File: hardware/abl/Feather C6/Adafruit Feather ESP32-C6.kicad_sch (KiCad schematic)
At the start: 43 parts, among them Q3 DMG3415U, SW1 KMR2, SW2 KMR2, U1 ESP32-C6-MINI_MINI, U2 AP2112/RT9080-3.3, U3 MCP73831T-2ACI/OT, U4 AHT20-F, U5 AP2112/RT9080-3.3, X1 JSTPH, X2 MAX17048/T, X3 USB C

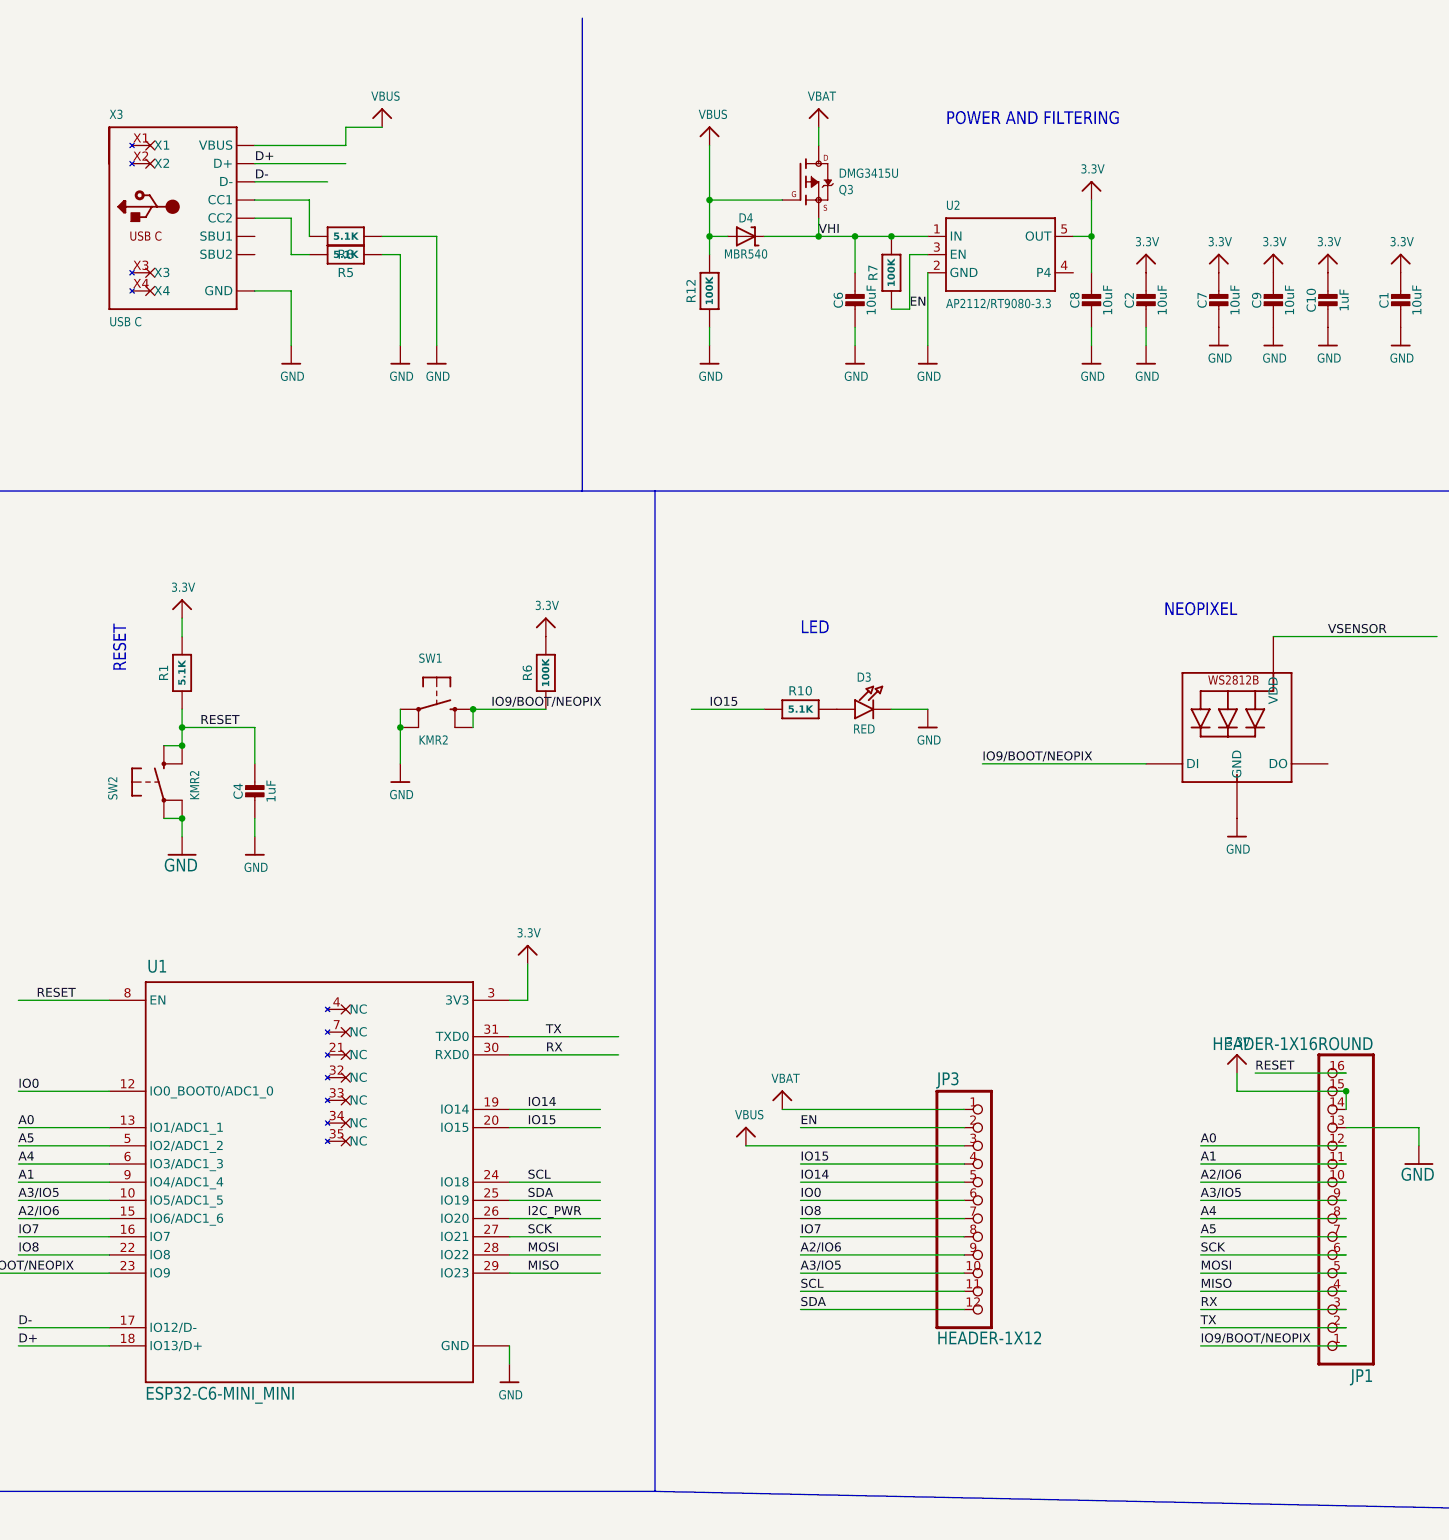
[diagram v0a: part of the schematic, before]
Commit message: Add ground planes and more ground pins.
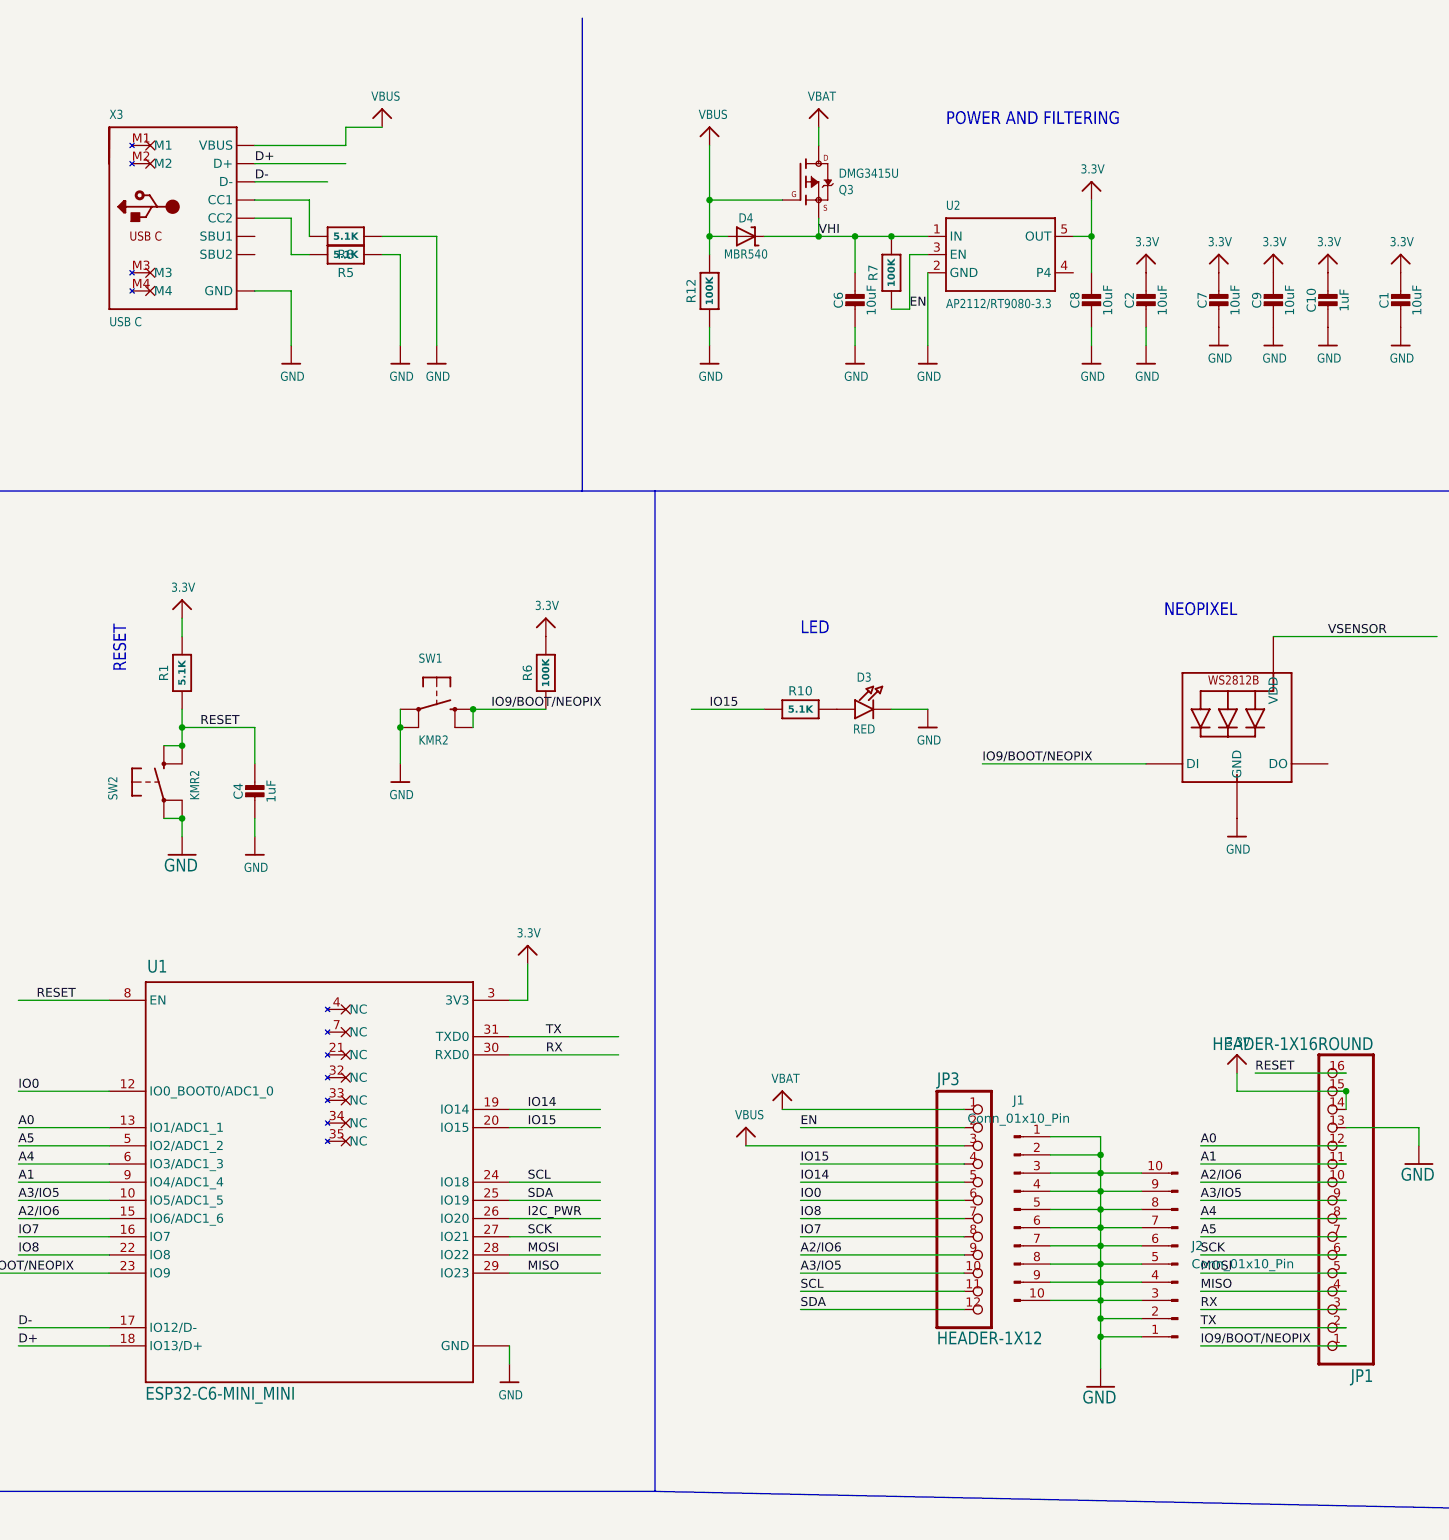
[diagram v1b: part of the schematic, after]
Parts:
- added J1, J2: Conn_01x10_Pin, Connector_PinHeader_2.54mm:PinHeader_1x10_P2.54mm_Vertical, symbol Connector:Conn_01x10_Pin
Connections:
- net GND: now also J1.1 (Pin_1), J1.10 (Pin_10), J1.2 (Pin_2), J1.3 (Pin_3), J1.4 (Pin_4), J1.5 (Pin_5), J1.6 (Pin_6), J1.7 (Pin_7), J1.8 (Pin_8), J1.9 (Pin_9), J2.1 (Pin_1), J2.10 (Pin_10), J2.2 (Pin_2), J2.3 (Pin_3), J2.4 (Pin_4), J2.5 (Pin_5), J2.6 (Pin_6), J2.7 (Pin_7), J2.8 (Pin_8), J2.9 (Pin_9)

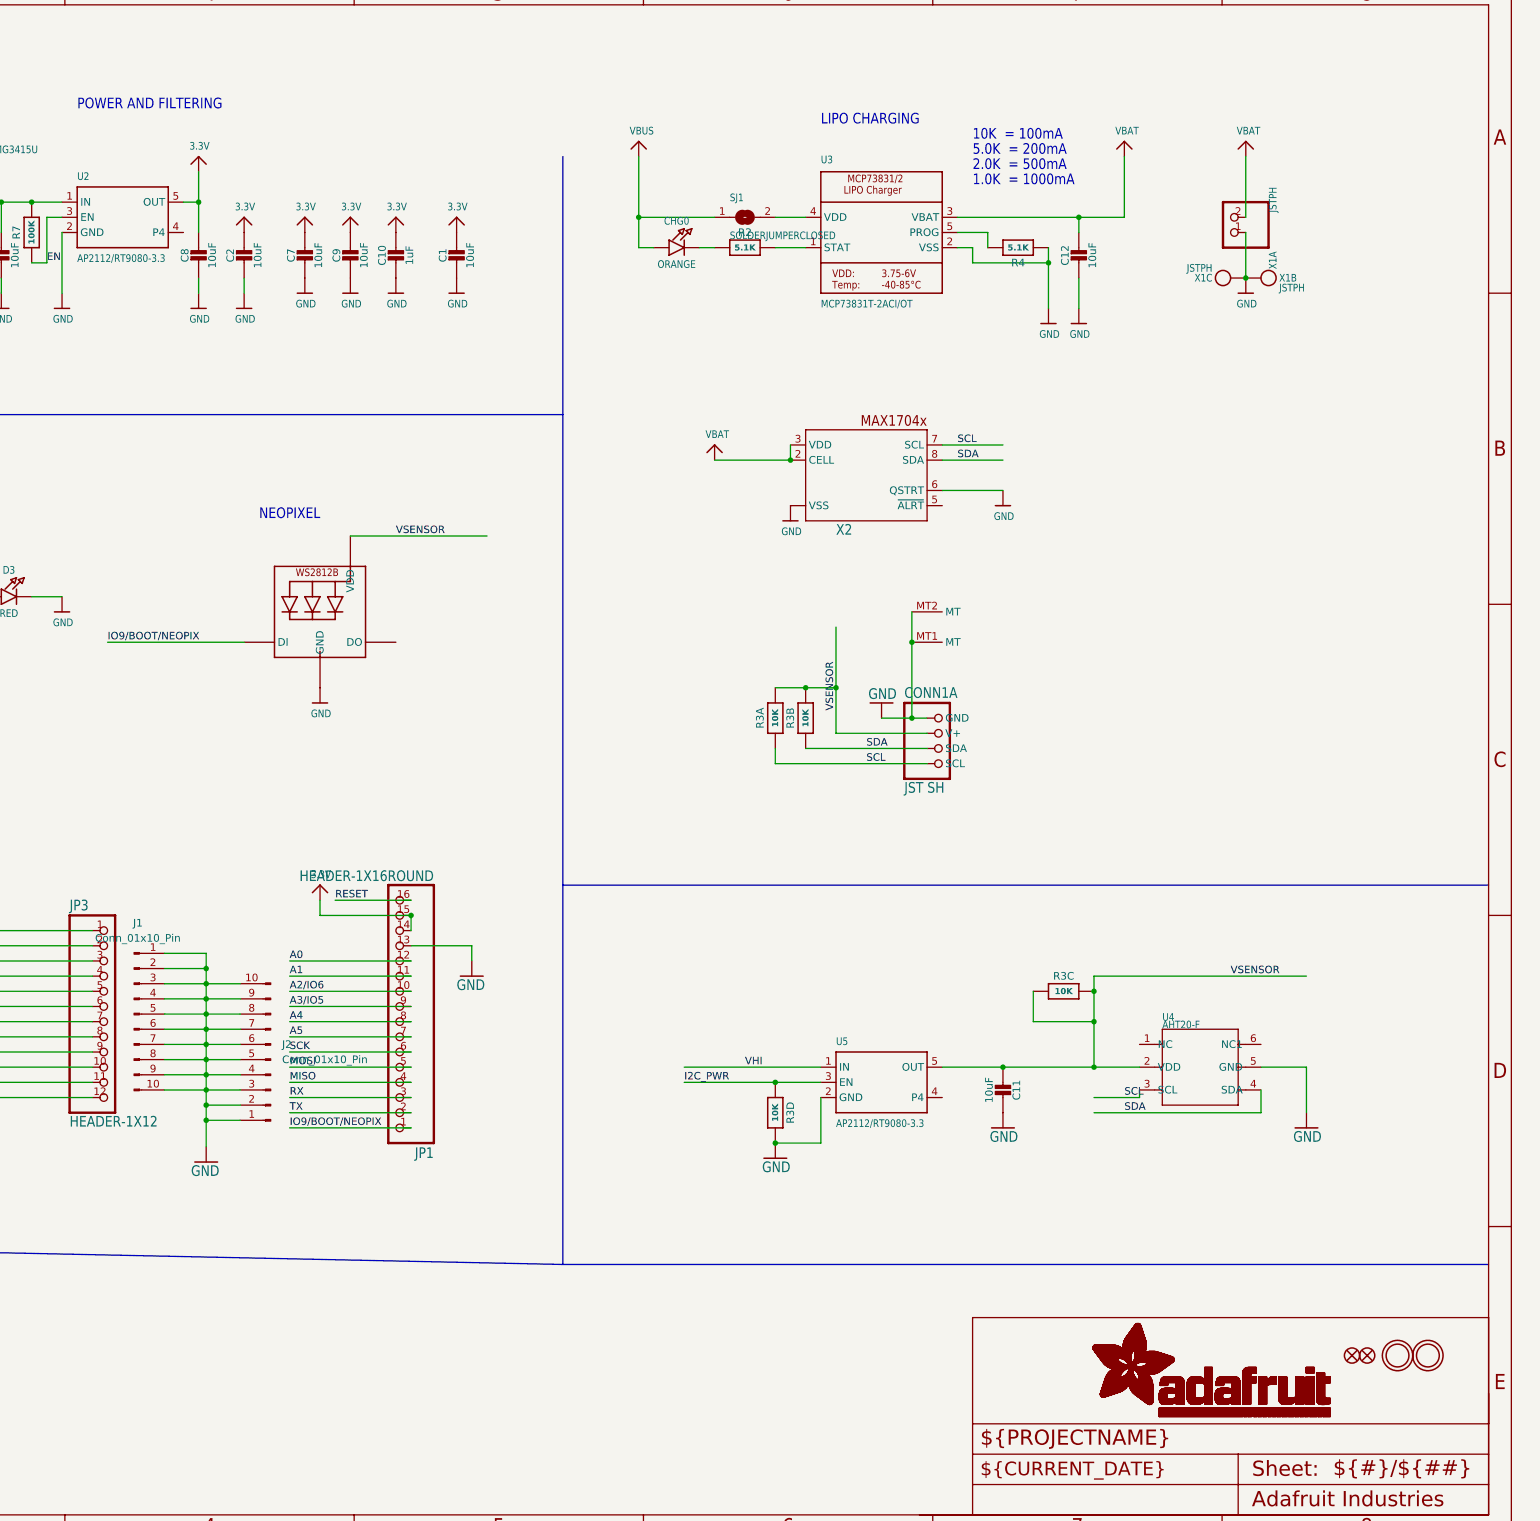
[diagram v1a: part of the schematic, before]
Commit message: Add Adafruit Feather ESP32-C6 version 1.1, originally made on 2025-01-05.
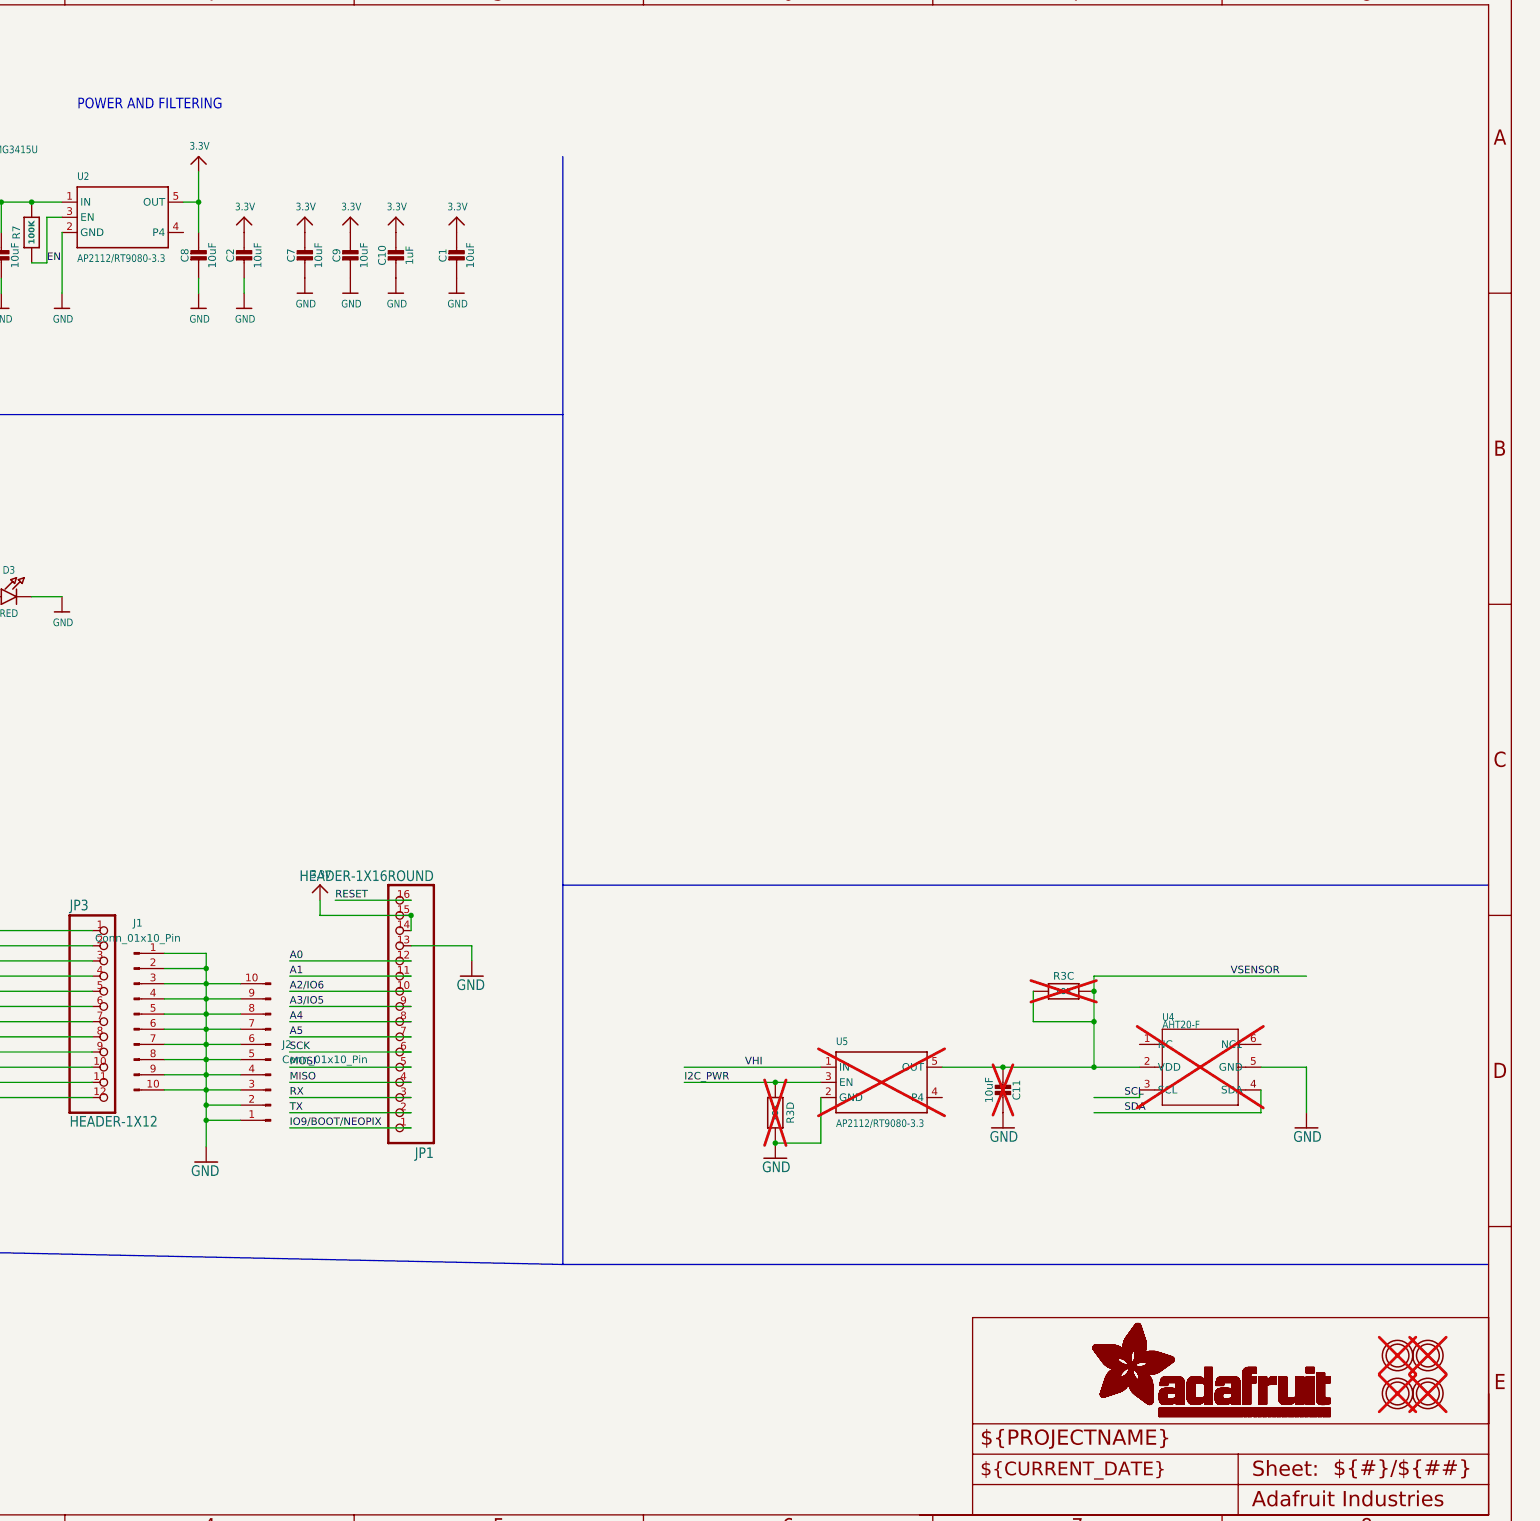
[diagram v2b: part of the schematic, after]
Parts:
- removed C12: 10uF, Adafruit Feather ESP32-C6:_0805MP, symbol Adafruit Feather ESP32-C6-eagle-import:CAP_CERAMIC_0805MP
- removed CHG0: ORANGE, Adafruit Feather ESP32-C6:CHIPLED_0603_NOOUTLINE, symbol Adafruit Feather ESP32-C6-eagle-import:LED0603_NOOUTLINE
- removed CONN1: JST SH, Adafruit Feather ESP32-C6:JST_SH4_RA, symbol Adafruit Feather ESP32-C6-eagle-import:STEMMA_I2C_QTRA
- removed LED1: WS2812B_3535FULL, Adafruit Feather ESP32-C6:LED3535_FULLPADS, symbol Adafruit Feather ESP32-C6-eagle-import:WS2812B_3535FULL
- removed R2, R4: 5.1K, Adafruit Feather ESP32-C6:0603-NO, symbol Adafruit Feather ESP32-C6-eagle-import:RESISTOR_0603_NOOUT
- removed unit 1 of R3
- removed unit 2 of R3
- removed SJ1: SOLDERJUMPERCLOSED, Adafruit Feather ESP32-C6:SOLDERJUMPER_CLOSEDWIRE, symbol Adafruit Feather ESP32-C6-eagle-import:SOLDERJUMPERCLOSED
- removed U$34, U$35: FIDUCIAL_1MM, Adafruit Feather ESP32-C6:FIDUCIAL_1MM, symbol Adafruit Feather ESP32-C6-eagle-import:FIDUCIAL_1MM
- removed U3: MCP73831T-2ACI/OT, Adafruit Feather ESP32-C6:SOT23-5, symbol Adafruit Feather ESP32-C6-eagle-import:MCP73831/2
- removed X1: JSTPH, Adafruit Feather ESP32-C6:JSTPH2_BATT, symbol Adafruit Feather ESP32-C6-eagle-import:CON_JST_PH_2PIN_MT_BATT
- removed X2: MAX17048/T, Adafruit Feather ESP32-C6:TDFN8_2X2MM, symbol Adafruit Feather ESP32-C6-eagle-import:MAX17048/T
- added U$1, U$2: MOUNTINGHOLE2.5, MountingHole:MountingHole_2.5mm, symbol Adafruit Feather ESP32-C6-eagle-import:MOUNTINGHOLE2.5
- C1, C2, C6, C7, C8, C9: footprint Adafruit Feather ESP32-C6:0805-NO -> Capacitor_SMD:C_0805_2012Metric; LCSC Part # (none) -> C15850
- C10, C4: footprint Adafruit Feather ESP32-C6:0603-NO -> Capacitor_SMD:C_0603_1608Metric; LCSC Part # (none) -> C15849
- C11, R3, U4, U5: now not fitted; now left out of the parts list
- D3: LCSC Part # (none) -> C7207730
- D4: LCSC Part # (none) -> C122863
- J1, J2: LCSC Part # (none) -> C2905418
- JP1: LCSC Part # (none) -> C2905421
- JP3: LCSC Part # (none) -> C2905419
- Q3: LCSC Part # (none) -> C7202986
- R1, R10, R5, R8: footprint Adafruit Feather ESP32-C6:0603-NO -> Resistor_SMD:R_0603_1608Metric; LCSC Part # (none) -> C23186
- R12, R6, R7: footprint Adafruit Feather ESP32-C6:0603-NO -> Resistor_SMD:R_0603_1608Metric; LCSC Part # (none) -> C25803
- SW1, SW2: LCSC Part # (none) -> C221676
- U$31, U$32: now not fitted
- U1: LCSC Part # (none) -> C5736265
- U2: LCSC Part # (none) -> C51118
- X3: LCSC Part # (none) -> C2927039
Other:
- note removed: "1.0K = 1000mA"
- note removed: "10K = 100mA"
- note removed: "2.0K = 500mA"
- note removed: "5.0K = 200mA"
- note removed: "LIPO CHARGING"
- note removed: "NEOPIXEL"
